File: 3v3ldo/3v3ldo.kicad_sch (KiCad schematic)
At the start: 3 parts

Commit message: Reapply "Update modules to kicad v7 format"
This reverts commit fa5cc85431189ac7a3beedf0871b5723203ae43f.
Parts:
- C101, C102: value (none) -> 1uF; footprint (none) -> Capacitor_SMD:C_0603_1608Metric
- U101: value (none) -> NCP1117-3.3_SOT223; footprint (none) -> Package_TO_SOT_SMD:SOT-223-3_TabPin2
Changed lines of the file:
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@@
-(kicad_sch (version 20211123) (generator eeschema)
+(kicad_sch (version 20230121) (generator eeschema)
   (paper "A4")
   (title_block
@@
   )
   (wire (pts (xy 161.29 93.98) (xy 161.29 90.17))
-    (stroke (width 0) (type default) (color 0 0 0 0))
+    (stroke (width 0) (type default))
   )
   (wire (pts (xy 129.54 101.6) (xy 146.05 101.6))
-    (stroke (width 0) (type default) (color 0 0 0 0))
+    (stroke (width 0) (type default))
   )
   (wire (pts (xy 129.54 101.6) (xy 116.84 101.6))
-    (stroke (width 0) (type default) (color 0 0 0 0))
+    (stroke (width 0) (type default))
   )
   (wire (pts (xy 138.43 90.17) (xy 129.54 90.17))
-    (stroke (width 0) (type default) (color 0 0 0 0))
+    (stroke (width 0) (type default))
   )
   (wire (pts (xy 129.54 90.17) (xy 116.84 90.17))
-    (stroke (width 0) (type default) (color 0 0 0 0))
+    (stroke (width 0) (type default))
   )
   (wire (pts (xy 161.29 90.17) (xy 172.72 90.17))
-    (stroke (width 0) (type default) (color 0 0 0 0))
+    (stroke (width 0) (type default))
   )
   (wire (pts (xy 129.54 99.06) (xy 129.54 101.6))
-    (stroke (width 0) (type default) (color 0 0 0 0))
+    (stroke (width 0) (type default))
   )
   (wire (pts (xy 146.05 101.6) (xy 161.29 101.6))
-    (stroke (width 0) (type default) (color 0 0 0 0))
+    (stroke (width 0) (type default))
   )
   (wire (pts (xy 129.54 90.17) (xy 129.54 93.98))
-    (stroke (width 0) (type default) (color 0 0 0 0))
+    (stroke (width 0) (type default))
   )
   (wire (pts (xy 161.29 101.6) (xy 161.29 99.06))
-    (stroke (width 0) (type default) (color 0 0 0 0))
+    (stroke (width 0) (type default))
   )
   (wire (pts (xy 146.05 97.79) (xy 146.05 101.6))
-    (stroke (width 0) (type default) (color 0 0 0 0))
+    (stroke (width 0) (type default))
   )
   (wire (pts (xy 161.29 90.17) (xy 153.67 90.17))
-    (stroke (width 0) (type default) (color 0 0 0 0))
+    (stroke (width 0) (type default))
   )
-  (hierarchical_label "GND" (shape passive) (at 116.84 101.6 180)
+  (hierarchical_label "GND" (shape passive) (at 116.84 101.6 180) (fields_autoplaced)
     (effects (font (size 1.27 1.27)) (justify right))
   )
-  (hierarchical_label "VOUT" (shape output) (at 172.72 90.17 0)
+  (hierarchical_label "VOUT" (shape output) (at 172.72 90.17 0) (fields_autoplaced)
     (effects (font (size 1.27 1.27)) (justify left))
   )
-  (hierarchical_label "VIN" (shape input) (at 116.84 90.17 180)
+  (hierarchical_label "VIN" (shape input) (at 116.84 90.17 180) (fields_autoplaced)
     (effects (font (size 1.27 1.27)) (justify right))
   )
   (symbol (lib_id "Regulator_Linear:NCP1117-3.3_SOT223") (at 146.05 90.17 0) (unit 1)
-    (in_bom yes) (on_board yes)
-    (property "Reference" "U101" (id 0) (at 146.05 84.0232 0))
-    (property "Value" "" (id 1) (at 146.05 86.3346 0))
-    (property "Footprint" "" (id 2) (at 146.05 85.09 0)
+    (in_bom yes) (on_board yes) (dnp no)
+    (property "Reference" "U101" (at 146.05 84.0232 0)
+      (effects (font (size 1.27 1.27)))
+    )
+    (property "Value" "NCP1117-3.3_SOT223" (at 146.05 86.3346 0)
+      (effects (font (size 1.27 1.27)))
+    )
+    (property "Footprint" "Package_TO_SOT_SMD:SOT-223-3_TabPin2" (at 146.05 85.09 0)
       (effects (font (size 1.27 1.27)) hide)
     )
-    (property "Datasheet" "http://www.onsemi.com/pub_link/Collateral/NCP1117-D.PDF" (id 3) (at 148.59 96.52 0)
+    (property "Datasheet" "http://www.onsemi.com/pub_link/Collateral/NCP1117-D.PDF" (at 148.59 96.52 0)
       (effects (font (size 1.27 1.27)) hide)
     )
@@
     (pin "2")
     (pin "3")
+    (instances
+      (project "3v3ldo"
+        (path "/554e6850-3780-446a-9126-30efe96707a4"
+          (reference "U101") (unit 1)
+        )
+      )
+    )
   )
   (symbol (lib_id "Device:C_Small") (at 129.54 96.52 0) (unit 1)
-    (in_bom yes) (on_board yes)
-    (property "Reference" "C101" (id 0) (at 131.8768 94.2086 0)
+    (in_bom yes) (on_board yes) (dnp no)
+    (property "Reference" "C101" (at 131.8768 94.2086 0)
       (effects (font (size 1.27 1.27)) (justify left))
     )
-    (property "Value" "" (id 1) (at 131.8768 96.52 0)
+    (property "Value" "1uF" (at 131.8768 96.52 0)
       (effects (font (size 1.27 1.27)) (justify left))
     )
-    (property "Footprint" "" (id 2) (at 129.54 96.52 0)
+    (property "Footprint" "Capacitor_SMD:C_0603_1608Metric" (at 129.54 96.52 0)
       (effects (font (size 1.27 1.27)) hide)
     )
-    (property "Datasheet" "~" (id 3) (at 129.54 96.52 0)
+    (property "Datasheet" "~" (at 129.54 96.52 0)
       (effects (font (size 1.27 1.27)) hide)
     )
-    (property "PartNo" "SomePartNumber" (id 4) (at 131.8768 98.8314 0)
+    (property "PartNo" "SomePartNumber" (at 131.8768 98.8314 0)
       (effects (font (size 1.27 1.27)) (justify left))
     )
     (pin "1")
     (pin "2")
+    (instances
+      (project "3v3ldo"
+        (path "/554e6850-3780-446a-9126-30efe96707a4"
+          (reference "C101") (unit 1)
+        )
+      )
+    )
   )
   (symbol (lib_id "Device:C_Small") (at 161.29 96.52 0) (unit 1)
-    (in_bom yes) (on_board yes)
-    (property "Reference" "C102" (id 0) (at 163.6268 94.2086 0)
+    (in_bom yes) (on_board yes) (dnp no)
+    (property "Reference" "C102" (at 163.6268 94.2086 0)
       (effects (font (size 1.27 1.27)) (justify left))
     )
-    (property "Value" "" (id 1) (at 163.6268 96.52 0)
+    (property "Value" "1uF" (at 163.6268 96.52 0)
       (effects (font (size 1.27 1.27)) (justify left))
     )
-    (property "Footprint" "" (id 2) (at 161.29 96.52 0)
+    (property "Footprint" "Capacitor_SMD:C_0603_1608Metric" (at 161.29 96.52 0)
       (effects (font (size 1.27 1.27)) hide)
     )
-    (property "Datasheet" "~" (id 3) (at 161.29 96.52 0)
+    (property "Datasheet" "~" (at 161.29 96.52 0)
       (effects (font (size 1.27 1.27)) hide)
     )
-    (property "PartNo" "SomePartNumber" (id 4) (at 163.6268 98.8314 0)
+    (property "PartNo" "SomePartNumber" (at 163.6268 98.8314 0)
       (effects (font (size 1.27 1.27)) (justify left))
     )
     (pin "1")
     (pin "2")
+    (instances
+      (project "3v3ldo"
+        (path "/554e6850-3780-446a-9126-30efe96707a4"
+          (reference "C102") (unit 1)
+        )
+      )
+    )
   )
   (sheet_instances
     (path "/" (page "1"))
   )
-  (symbol_instances
-    (path "/00000000-0000-0000-0000-00005e248390"
-      (reference "C101") (unit 1) (value "1uF") (footprint "Capacitor_SMD:C_0603_1608Metric")
-    )
-    (path "/00000000-0000-0000-0000-00005e24895c"
-      (reference "C102") (unit 1) (value "1uF") (footprint "Capacitor_SMD:C_0603_1608Metric")
-    )
-    (path "/00000000-0000-0000-0000-00005e246b49"
-      (reference "U101") (unit 1) (value "NCP1117-3.3_SOT223") (footprint "Package_TO_SOT_SMD:SOT-223-3_TabPin2")
-    )
-  )
 )

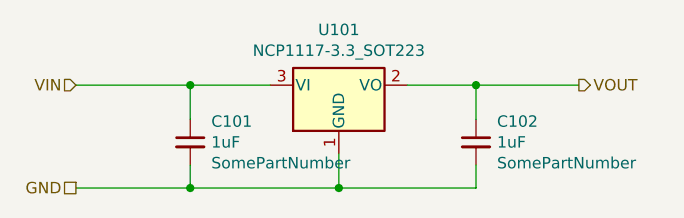
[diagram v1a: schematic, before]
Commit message: Revert "Update modules to kicad v7 format"
This reverts commit 3325eb02d48d3d222bc7f8945228a1814ae85736.
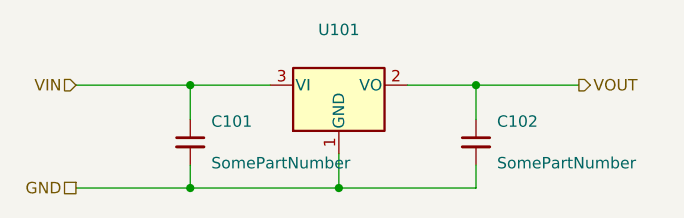
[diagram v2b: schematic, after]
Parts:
- C101, C102: value 1uF -> (none); footprint Capacitor_SMD:C_0603_1608Metric -> (none)
- U101: value NCP1117-3.3_SOT223 -> (none); footprint Package_TO_SOT_SMD:SOT-223-3_TabPin2 -> (none)
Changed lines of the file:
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@@
-(kicad_sch (version 20230121) (generator eeschema)
+(kicad_sch (version 20211123) (generator eeschema)
   (paper "A4")
   (title_block
@@
   )
   (wire (pts (xy 161.29 93.98) (xy 161.29 90.17))
-    (stroke (width 0) (type default))
+    (stroke (width 0) (type default) (color 0 0 0 0))
   )
   (wire (pts (xy 129.54 101.6) (xy 146.05 101.6))
-    (stroke (width 0) (type default))
+    (stroke (width 0) (type default) (color 0 0 0 0))
   )
   (wire (pts (xy 129.54 101.6) (xy 116.84 101.6))
-    (stroke (width 0) (type default))
+    (stroke (width 0) (type default) (color 0 0 0 0))
   )
   (wire (pts (xy 138.43 90.17) (xy 129.54 90.17))
-    (stroke (width 0) (type default))
+    (stroke (width 0) (type default) (color 0 0 0 0))
   )
   (wire (pts (xy 129.54 90.17) (xy 116.84 90.17))
-    (stroke (width 0) (type default))
+    (stroke (width 0) (type default) (color 0 0 0 0))
   )
   (wire (pts (xy 161.29 90.17) (xy 172.72 90.17))
-    (stroke (width 0) (type default))
+    (stroke (width 0) (type default) (color 0 0 0 0))
   )
   (wire (pts (xy 129.54 99.06) (xy 129.54 101.6))
-    (stroke (width 0) (type default))
+    (stroke (width 0) (type default) (color 0 0 0 0))
   )
   (wire (pts (xy 146.05 101.6) (xy 161.29 101.6))
-    (stroke (width 0) (type default))
+    (stroke (width 0) (type default) (color 0 0 0 0))
   )
   (wire (pts (xy 129.54 90.17) (xy 129.54 93.98))
-    (stroke (width 0) (type default))
+    (stroke (width 0) (type default) (color 0 0 0 0))
   )
   (wire (pts (xy 161.29 101.6) (xy 161.29 99.06))
-    (stroke (width 0) (type default))
+    (stroke (width 0) (type default) (color 0 0 0 0))
   )
   (wire (pts (xy 146.05 97.79) (xy 146.05 101.6))
-    (stroke (width 0) (type default))
+    (stroke (width 0) (type default) (color 0 0 0 0))
   )
   (wire (pts (xy 161.29 90.17) (xy 153.67 90.17))
-    (stroke (width 0) (type default))
+    (stroke (width 0) (type default) (color 0 0 0 0))
   )
-  (hierarchical_label "GND" (shape passive) (at 116.84 101.6 180) (fields_autoplaced)
+  (hierarchical_label "GND" (shape passive) (at 116.84 101.6 180)
     (effects (font (size 1.27 1.27)) (justify right))
   )
-  (hierarchical_label "VOUT" (shape output) (at 172.72 90.17 0) (fields_autoplaced)
+  (hierarchical_label "VOUT" (shape output) (at 172.72 90.17 0)
     (effects (font (size 1.27 1.27)) (justify left))
   )
-  (hierarchical_label "VIN" (shape input) (at 116.84 90.17 180) (fields_autoplaced)
+  (hierarchical_label "VIN" (shape input) (at 116.84 90.17 180)
     (effects (font (size 1.27 1.27)) (justify right))
   )
   (symbol (lib_id "Regulator_Linear:NCP1117-3.3_SOT223") (at 146.05 90.17 0) (unit 1)
-    (in_bom yes) (on_board yes) (dnp no)
-    (property "Reference" "U101" (at 146.05 84.0232 0)
-      (effects (font (size 1.27 1.27)))
-    )
-    (property "Value" "NCP1117-3.3_SOT223" (at 146.05 86.3346 0)
-      (effects (font (size 1.27 1.27)))
-    )
-    (property "Footprint" "Package_TO_SOT_SMD:SOT-223-3_TabPin2" (at 146.05 85.09 0)
+    (in_bom yes) (on_board yes)
+    (property "Reference" "U101" (id 0) (at 146.05 84.0232 0))
+    (property "Value" "" (id 1) (at 146.05 86.3346 0))
+    (property "Footprint" "" (id 2) (at 146.05 85.09 0)
       (effects (font (size 1.27 1.27)) hide)
     )
-    (property "Datasheet" "http://www.onsemi.com/pub_link/Collateral/NCP1117-D.PDF" (at 148.59 96.52 0)
+    (property "Datasheet" "http://www.onsemi.com/pub_link/Collateral/NCP1117-D.PDF" (id 3) (at 148.59 96.52 0)
       (effects (font (size 1.27 1.27)) hide)
     )
@@
     (pin "2")
     (pin "3")
-    (instances
-      (project "3v3ldo"
-        (path "/554e6850-3780-446a-9126-30efe96707a4"
-          (reference "U101") (unit 1)
-        )
-      )
-    )
   )
   (symbol (lib_id "Device:C_Small") (at 129.54 96.52 0) (unit 1)
-    (in_bom yes) (on_board yes) (dnp no)
-    (property "Reference" "C101" (at 131.8768 94.2086 0)
+    (in_bom yes) (on_board yes)
+    (property "Reference" "C101" (id 0) (at 131.8768 94.2086 0)
       (effects (font (size 1.27 1.27)) (justify left))
     )
-    (property "Value" "1uF" (at 131.8768 96.52 0)
+    (property "Value" "" (id 1) (at 131.8768 96.52 0)
       (effects (font (size 1.27 1.27)) (justify left))
     )
-    (property "Footprint" "Capacitor_SMD:C_0603_1608Metric" (at 129.54 96.52 0)
+    (property "Footprint" "" (id 2) (at 129.54 96.52 0)
       (effects (font (size 1.27 1.27)) hide)
     )
-    (property "Datasheet" "~" (at 129.54 96.52 0)
+    (property "Datasheet" "~" (id 3) (at 129.54 96.52 0)
       (effects (font (size 1.27 1.27)) hide)
     )
-    (property "PartNo" "SomePartNumber" (at 131.8768 98.8314 0)
+    (property "PartNo" "SomePartNumber" (id 4) (at 131.8768 98.8314 0)
       (effects (font (size 1.27 1.27)) (justify left))
     )
     (pin "1")
     (pin "2")
-    (instances
-      (project "3v3ldo"
-        (path "/554e6850-3780-446a-9126-30efe96707a4"
-          (reference "C101") (unit 1)
-        )
-      )
-    )
   )
   (symbol (lib_id "Device:C_Small") (at 161.29 96.52 0) (unit 1)
-    (in_bom yes) (on_board yes) (dnp no)
-    (property "Reference" "C102" (at 163.6268 94.2086 0)
+    (in_bom yes) (on_board yes)
+    (property "Reference" "C102" (id 0) (at 163.6268 94.2086 0)
       (effects (font (size 1.27 1.27)) (justify left))
     )
-    (property "Value" "1uF" (at 163.6268 96.52 0)
+    (property "Value" "" (id 1) (at 163.6268 96.52 0)
       (effects (font (size 1.27 1.27)) (justify left))
     )
-    (property "Footprint" "Capacitor_SMD:C_0603_1608Metric" (at 161.29 96.52 0)
+    (property "Footprint" "" (id 2) (at 161.29 96.52 0)
       (effects (font (size 1.27 1.27)) hide)
     )
-    (property "Datasheet" "~" (at 161.29 96.52 0)
+    (property "Datasheet" "~" (id 3) (at 161.29 96.52 0)
       (effects (font (size 1.27 1.27)) hide)
     )
-    (property "PartNo" "SomePartNumber" (at 163.6268 98.8314 0)
+    (property "PartNo" "SomePartNumber" (id 4) (at 163.6268 98.8314 0)
       (effects (font (size 1.27 1.27)) (justify left))
     )
     (pin "1")
     (pin "2")
-    (instances
-      (project "3v3ldo"
-        (path "/554e6850-3780-446a-9126-30efe96707a4"
-          (reference "C102") (unit 1)
-        )
-      )
-    )
   )
   (sheet_instances
     (path "/" (page "1"))
   )
+  (symbol_instances
+    (path "/00000000-0000-0000-0000-00005e248390"
+      (reference "C101") (unit 1) (value "1uF") (footprint "Capacitor_SMD:C_0603_1608Metric")
+    )
+    (path "/00000000-0000-0000-0000-00005e24895c"
+      (reference "C102") (unit 1) (value "1uF") (footprint "Capacitor_SMD:C_0603_1608Metric")
+    )
+    (path "/00000000-0000-0000-0000-00005e246b49"
+      (reference "U101") (unit 1) (value "NCP1117-3.3_SOT223") (footprint "Package_TO_SOT_SMD:SOT-223-3_TabPin2")
+    )
+  )
 )
